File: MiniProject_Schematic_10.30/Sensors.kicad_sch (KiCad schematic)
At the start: 26 parts, among them U4 VEML3328, U5 TMAG5273C1QDBVR, U6 LM75ADP, U7 TCA9534PWR

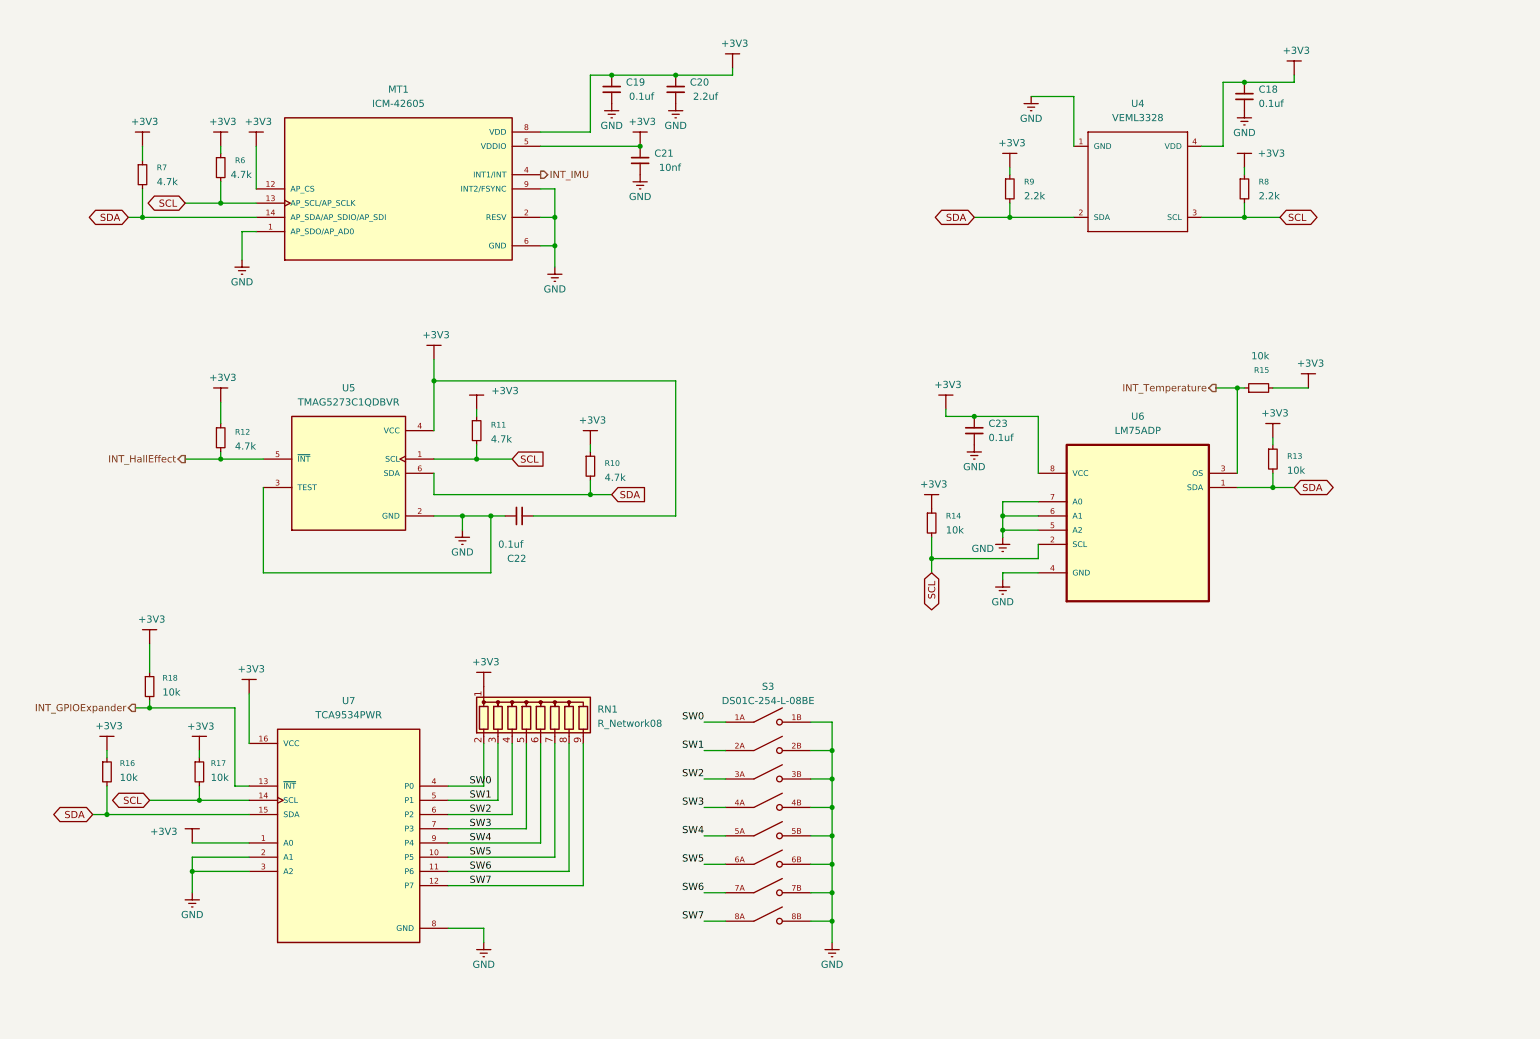
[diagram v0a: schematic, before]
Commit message: Correct the schematic diagram
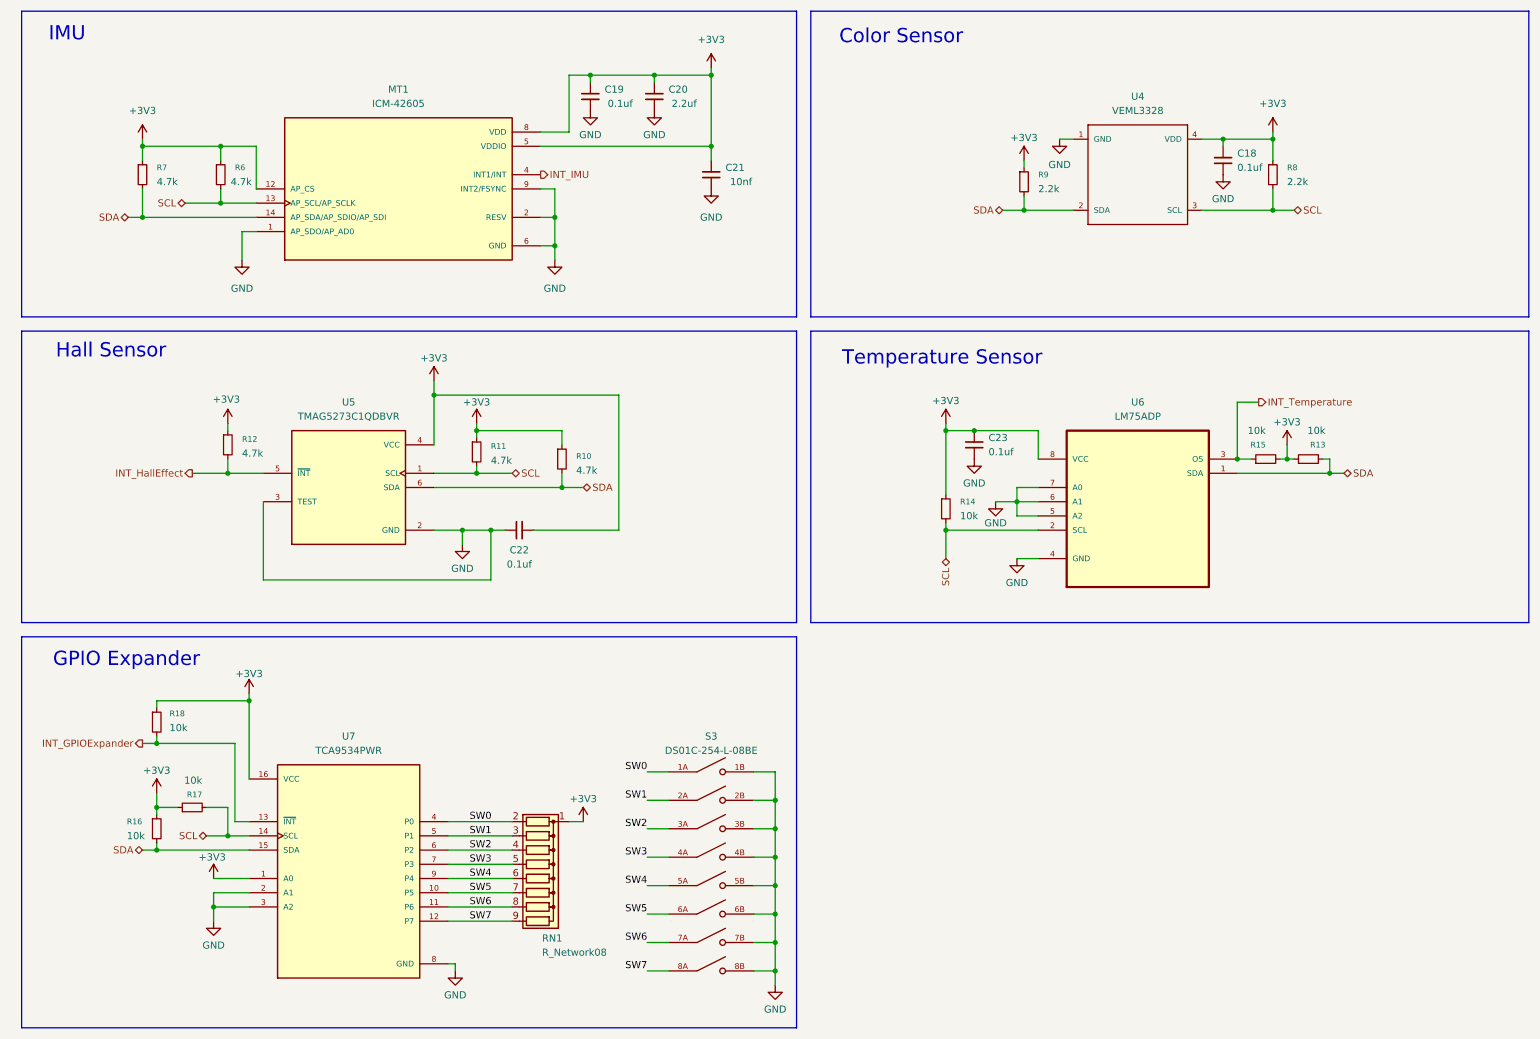
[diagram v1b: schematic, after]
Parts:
- C22: value C_Small -> 0.1uf; Capacitance 0.1uf -> (none)
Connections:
- net +3V3: now also C22.1; no longer C22.2
- net GND: now also C22.2; no longer C22.1
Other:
- note added: "Color Sensor"
- note added: "GPIO Expander"
- note added: "Hall Sensor"
- note added: "IMU"
- note added: "Temperature Sensor"
- moved on the sheet: C18, C19, C20, C21, C23, R10, R11, R12, R13, R14, R15, R16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
